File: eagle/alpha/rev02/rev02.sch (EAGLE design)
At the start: 382 parts, among them CN1 HOST, CN2 HOST, IC1 N25Q128A13ES, IC2 74AC244DW, IC3 N25Q128A13ES, J1 STM32-SWD, Q1 2N7002, Q2 BC818, Q4 2N7002, Q5 ASFL1, Q6 2N7002, T1 BC847, T2 BC847, U1 LMZ13608, U10 ATTINY828R-AU, U11 MC14551BDG, U12 23K640-I/SN, U13 XC7A200TFBG484, U14 EN6347QI, U15 EN6347QI, U16 EN5364QI, U2 LT3060ITS8-15, U3 MC74HC1G14DTT1G, U4 STM32F429BIT6, U5 IS45S32160F, U6 IS45S32160F, U7 MCP79412-I/SN, U8 FT232H_SERIAL, U9 FT232H_SERIAL, Y1 12 MHz, Y2 12 MHz

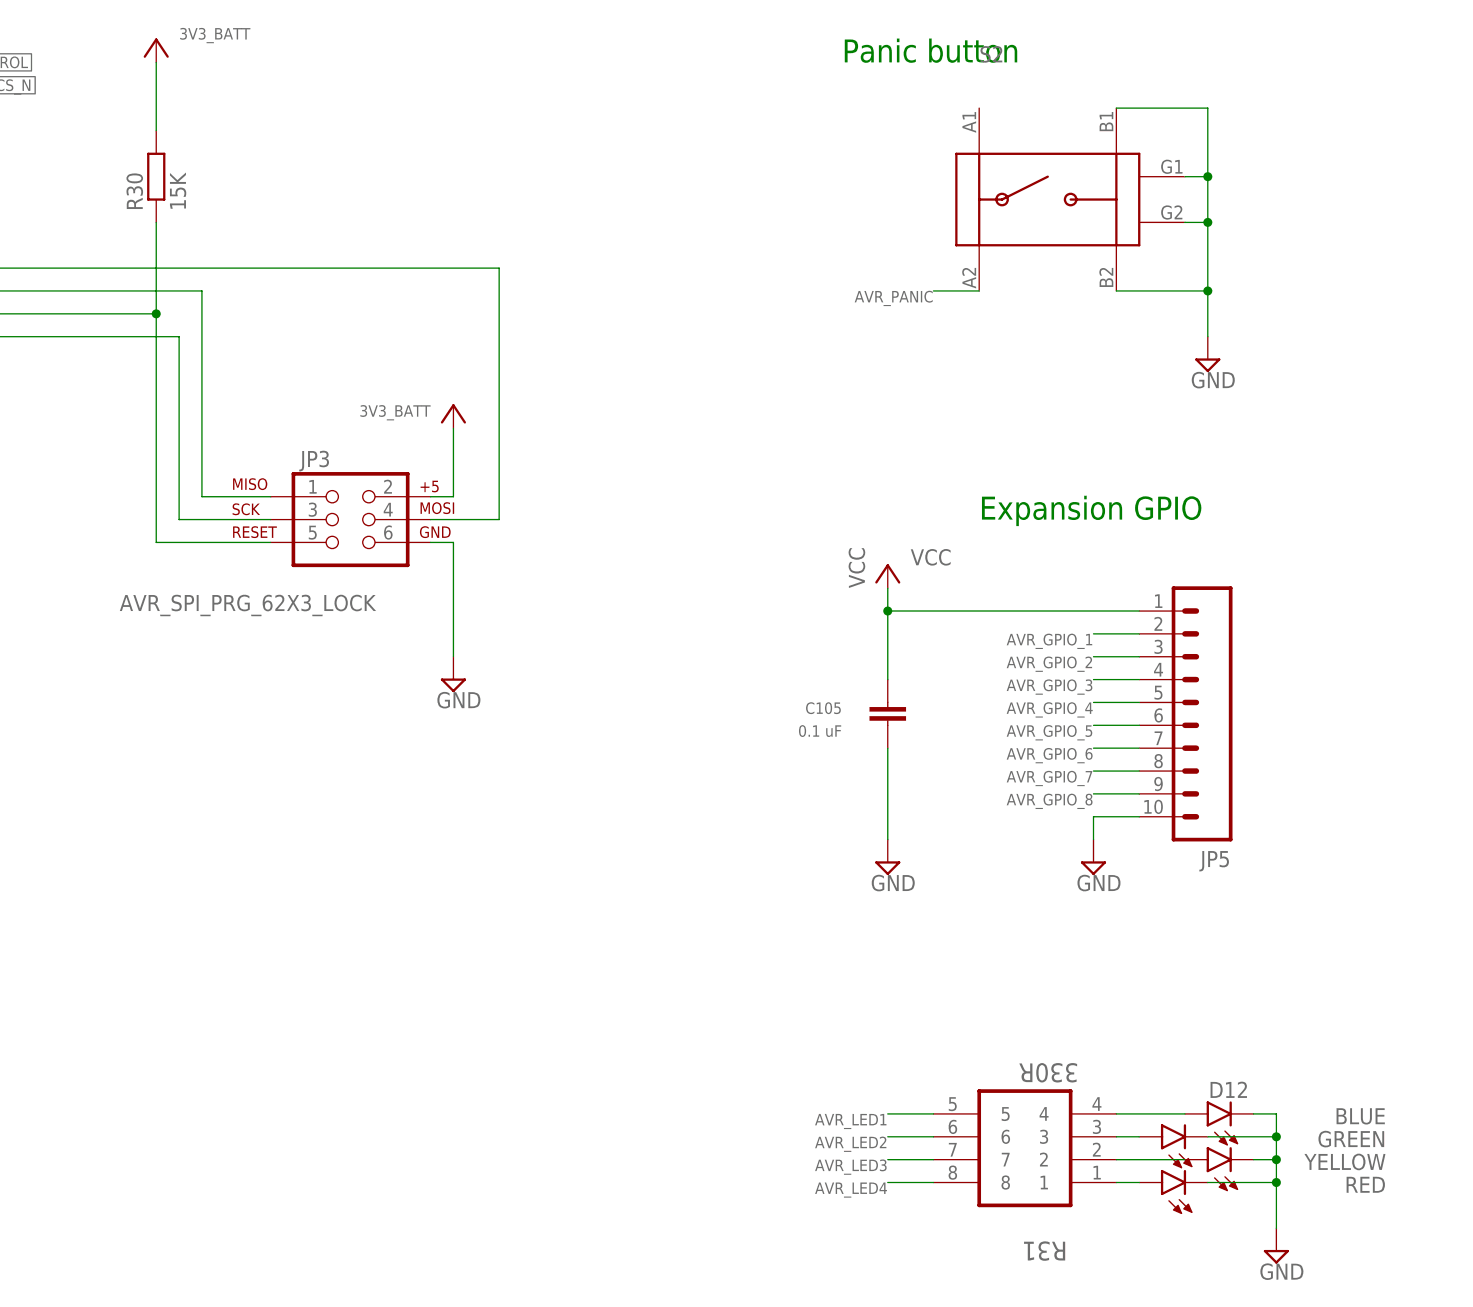
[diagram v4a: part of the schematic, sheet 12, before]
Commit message: optimize BOM a bit, change more 0603s to 0402s
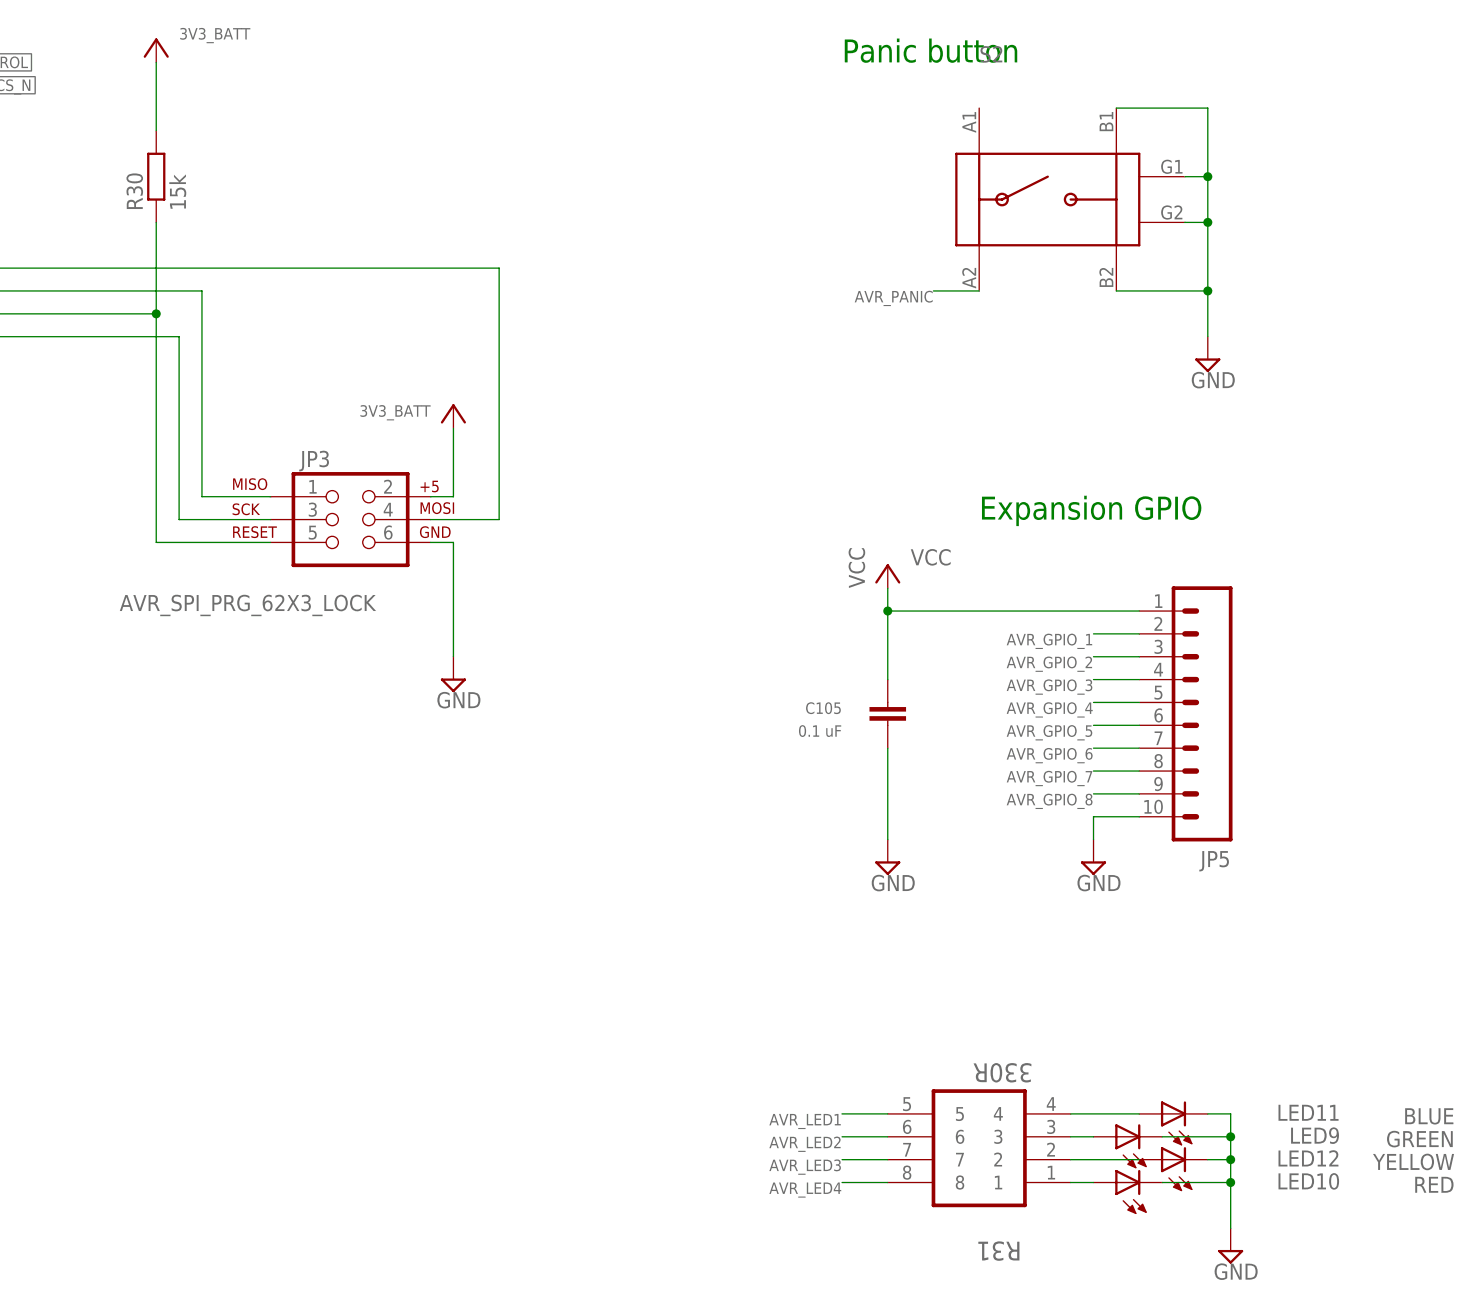
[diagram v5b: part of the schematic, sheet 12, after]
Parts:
- removed D10, D7, D9: GREEN, SparkFun-LED:LED0603
- removed D11: RED, SparkFun-LED:LED0603
- removed D12: BLUE, SparkFun-LED:LED0603
- removed D13, D5, D6, D8: YELLOW, SparkFun-LED:LED0603
- removed D14, D15, D16: BAT54, diode:BAT54
- added LED10, LED13, LED14: RED, led:LEDCHIP-LED0603
- added LED11, LED17: BLUE, led:LEDCHIP-LED0603
- added LED12, LED16, LED7: YELLOW, led:LEDCHIP-LED0603
- added LED15, LED18, LED8, LED9: GREEN, led:LEDCHIP-LED0603
- C10, C9: value 330uF -> 330 uF
- C108, C109, C111, C112, C117, C118, C121, C122, C208, C211, C212, C213, C69: device resistor:C-EUC0603 -> resistor:C-EUC0402
- C11, C12: value 10NF -> 0.01 uF
- C110: value 0.1uF -> 0.1 uF; DIELECTRIC (none) -> X7R; RATED_VOLTAGE (none) -> 10V
- C115, C116, C207, C4, C6: value 0.047uF -> 0.047 uF; device resistor:C-EUC0603 -> resistor:C-EUC0402
- C13, C7: value 2.2 uF LowESR -> 2.2 uF
- C14, C15, C16: device rcl:C-EUC0603 -> resistor:C-EUC0603; DIELECTRIC (none) -> X7R; RATED_VOLTAGE (none) -> 50V; TOLERANCE (none) -> 10%
- C19, C20, C30, C32, C33, C34, C35, C36, C37, C38, C39, C40, C41, C42, C43, C44, C45, C46, C49, C51, C52, C53, C54, C55, C56, C57, C60, C62, C63, C64, C65, C66, C67, C68: value 0.1uF -> 0.1 uF
- C5: value 0.47uF -> 0.47 uF
- C70, C71: value 5pF -> 5 pF; device rcl:C-EUC0603 -> resistor:C-EUC0402; DIELECTRIC (none) -> C0G; RATED_VOLTAGE (none) -> 10V
- C75, C78, C90, C93: device rcl:C-EUC0603 -> resistor:C-EUC0402
- D2: value GREEN -> BAT54; device SparkFun-LED:LED0603 -> diode:BAT54
- D3: value RED -> BAT54; device SparkFun-LED:LED0603 -> diode:BAT54
- D4: value BLUE -> BAT54; device SparkFun-LED:LED0603 -> diode:BAT54
- LED1: value RED -> GREEN
- LED3: value GREEN -> BLUE
- LED5: value BLUE -> YELLOW
- R1, R17, R18, R2, R3, R35, R36, R37, R38, R39, R4, R40, R41, R42, R43, R44, R45, R49, R50, R51, R52, R53, R54, R55, R56, R57, R58, R59, R60, R61, R65, R66, R67, R68, R69, R70, R72, R73, R74, R75, R76, R77, R78, R8, R9: device resistor:R-EU_R0603 -> resistor:R-EU_R0402
- R10: device resistor:R-EU_R0603 -> resistor:R-EU_R0402; TOLERANCE (none) -> 1%
- R11, R13: value 1K -> 1k; device resistor:R-EU_R0603 -> resistor:R-EU_R0402; TOLERANCE (none) -> 1%
- R12: value 10K -> 10k; device resistor:R-EU_R0603 -> resistor:R-EU_R0402; TOLERANCE (none) -> 1%
- R15, R19, R20, R21, R23, R27, R7: value 10K -> 10k; TOLERANCE (none) -> 5%
- R22, R26: value 12K -> 12k
- R24, R25, R28, R29: TOLERANCE (none) -> 5%
- R30: value 15K -> 15k
- R32, R33, R34: value 15K -> 15k; device resistor:R-EU_R0603 -> resistor:R-EU_R0402
- R46, R47, R48: device resistor:R-EU_R0603 -> resistor:R-EU_R0402; TOLERANCE (none) -> 5%
- R5: value 1K -> 1k
- R6: value 10K -> 10k
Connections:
- net FPGA_DONE_INT: now also LED13.C; no longer LED1.C
- net FT_MGMT_VCC3V3: now also LED7.A, LED8.A; no longer D8.A, D9.A
- net FT_VCC3V3: now also LED5.A, LED6.A; no longer D6.A, D7.A
- net GND: now also LED1.C, LED10.C, LED11.C, LED12.C, LED14.C, LED15.C, LED16.C, LED17.C, LED9.C; no longer D10.C, D11.C, D12.C, D13.C, D2.C, D3.C, D4.C, D5.C, LED5.C
- net N$15: now also LED12.A; no longer D13.A
- net N$16: now also LED10.A; no longer D11.A
- net N$17: now also LED3.A; no longer D4.A
- net N$18: now also LED1.A; no longer D2.A
- net N$19: now also LED4.A; no longer D5.A
- net N$20: now also LED2.A; no longer D3.A
- net N$24: now also LED5.C; no longer D6.C
- net N$26: now also LED6.C; no longer D7.C
- net N$27: now also LED17.A; no longer LED5.A
- net N$28: now also LED15.A; no longer LED3.A
- net N$29: now also LED16.A; no longer LED4.A
- net N$30: now also LED14.A; no longer LED2.A
- net N$34: now also LED13.A; no longer LED1.A
- net N$4: now also LED11.A; no longer D12.A
- net N$5: now also LED9.A; no longer D10.A
- net N$50: now also LED18.C; no longer LED6.C
- net N$51: now also LED18.A; no longer LED6.A
- net N$6: now also LED7.C; no longer D8.C
- net N$7: now also LED8.C; no longer D9.C
- net POK_VCCAUX: now also D3.C; no longer D15.C
- net POK_VCCINT: now also D4.C; no longer D16.C
- net PWR_ENA_VCCAUX: now also D4.A; no longer D16.A
- net PWR_ENA_VCCINT: now also D2.A; no longer D14.A
- net PWR_ENA_VCCO: now also D3.A; no longer D15.A
- net VCC_5V0: now also D2.C; no longer D14.C
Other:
- note added: "XXX verify symbol"
- moved on the sheet: C14, D1, R31, TP2
